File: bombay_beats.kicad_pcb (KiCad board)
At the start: 2 copper layers, 154.9 x 17.8 mm, 22 parts, among them SW1 SW_SPDT, U1 74HC165

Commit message: one sided version
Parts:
- added C1: 0.1u, Capacitor_SMD:C_0201_0603Metric, F.Cu at (129.5, 81.3)
- SW1, U1, jst_in1, jst_out1, solder_in1, solder_out1: moved to F.Cu
- moved SW1 38.2 mm to (132.3, 86.2), turned to 0 degrees
- moved R8 14.4 mm to (185.3, 76.8)
- moved btn_8 14.4 mm to (182.6, 85.0)
- moved solder_in1 12.5 mm to (194.0, 76.7), turned to 0 degrees
- moved btn_1 12.3 mm to (82.0, 85.0)
- moved R1 12.3 mm to (84.7, 76.8)
- moved jst_out1 12.0 mm to (60.9, 81.8), turned to -90 degrees
- moved jst_in1 9.95 mm to (203.7, 81.9), turned to 90 degrees
- moved R7 9.41 mm to (172.1, 76.8)
- moved btn_7 9.41 mm to (169.4, 85.0)
- moved solder_out1 9.32 mm to (69.5, 76.7), turned to 0 degrees
- moved R2 7.32 mm to (97.9, 76.8)
- moved btn_2 7.32 mm to (95.2, 85.0)
- moved U1 5.09 mm to (132.5, 77.7)
- moved R6 4.48 mm to (158.9, 76.8)
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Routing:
- net VCC: track 198.2 -> 328.8 mm, vias 3 -> 2
- net /DATA_IN: track 37.7 -> 78.8 mm
- net Net-(SW1-B): track 52.2 -> 19.9 mm
- net /DATA_CLK: track 171.7 -> 153.9 mm, vias 4 -> 0
- net /DATA_LOAD: track 162.8 -> 146.5 mm, vias 5 -> 2
- net GND: track 52.8 -> 37.4 mm, vias 8 -> 13
- net /Button Module/data: track 65.9 -> 51.9 mm, vias 1 -> 2
- net /Button Module7/data: track 59.1 -> 49.6 mm, vias 1 -> 0
- net /Button Module1/data: track 47.1 -> 38.3 mm, vias 1 -> 2
- net /Button Module6/data: track 40.7 -> 34.3 mm, vias 1 -> 0
- net /DATA_OUT: track 82.4 -> 86.4 mm
- net /Button Module2/data: track 28.6 -> 24.8 mm, vias 1 -> 2
- net /Button Module5/data: track 22.2 -> 19.6 mm, vias 1 -> 0
- net /Button Module3/data: track 10.1 -> 12.0 mm, vias 1 -> 0
- net /Button Module4/data: track 4.81 -> 4.69 mm, vias 1 -> 0

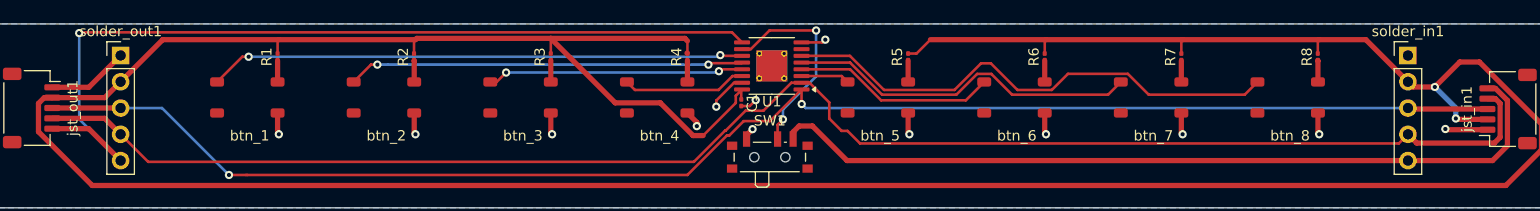
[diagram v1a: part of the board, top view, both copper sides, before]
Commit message: finalize one sided smd version
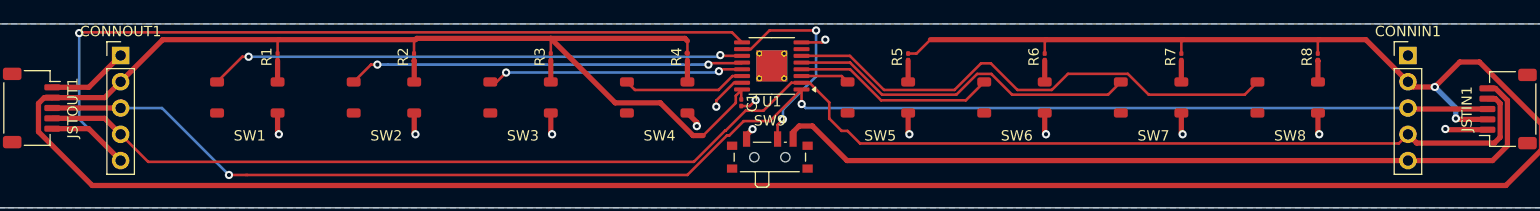
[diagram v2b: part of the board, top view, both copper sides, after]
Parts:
- renumbered solder_in1 to CONNIN1, solder_out1 to CONNOUT1, jst_in1 to JSTIN1, jst_out1 to JSTOUT1, btn_1 to SW1, btn_2 to SW2, btn_3 to SW3, btn_4 to SW4, btn_5 to SW5, btn_6 to SW6, btn_7 to SW7, btn_8 to SW8, SW1 to SW9

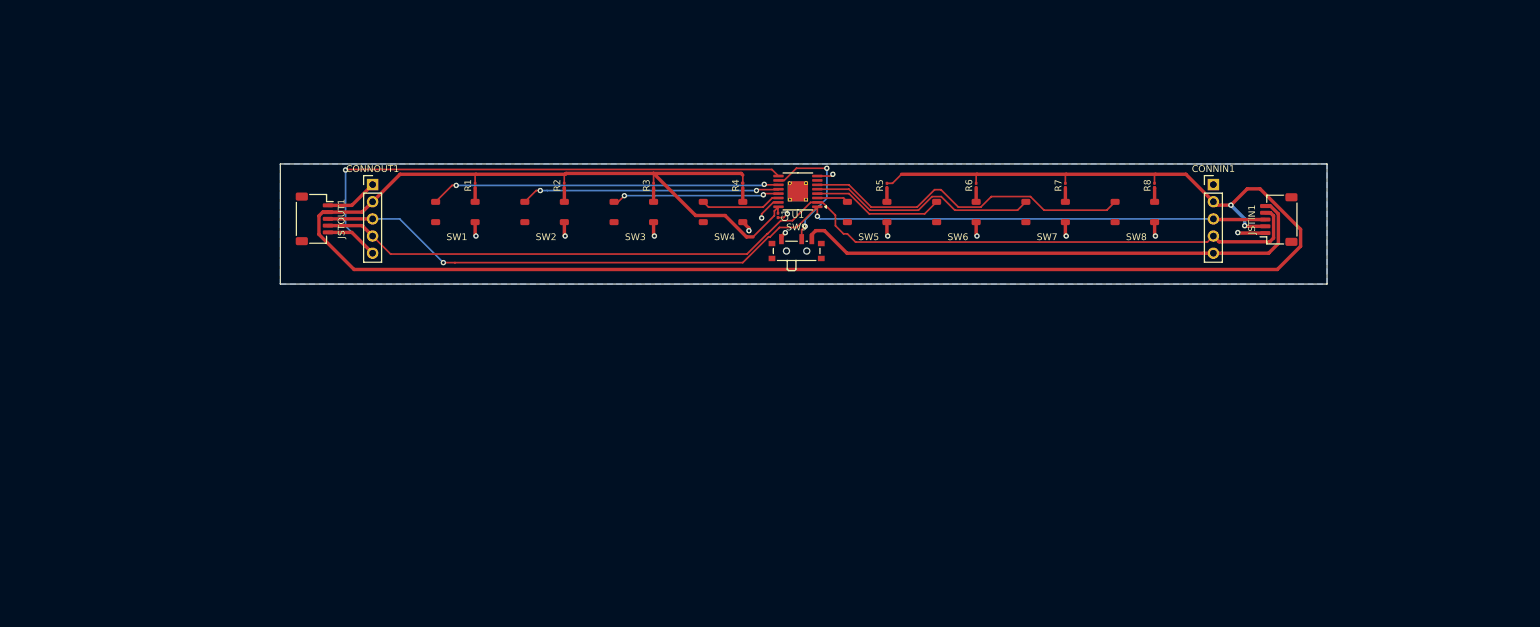
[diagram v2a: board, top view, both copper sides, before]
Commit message: replace footprints for through hole version
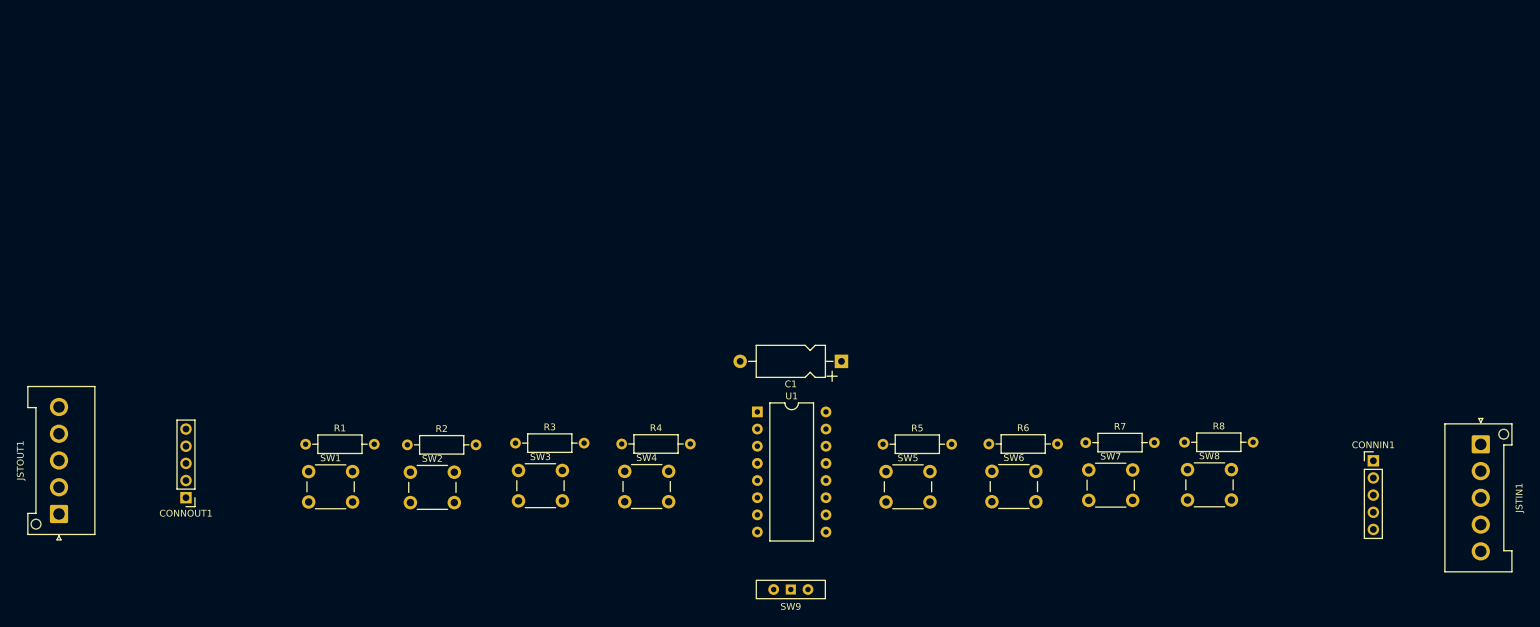
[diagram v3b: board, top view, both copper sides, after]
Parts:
- C1: footprint Capacitor_SMD:C_0201_0603Metric -> Capacitor_THT:CP_Axial_L10.0mm_D4.5mm_P15.00mm_Horizontal
- JSTIN1, JSTOUT1: footprint Connector_JST:JST_SH_SM05B-SRSS-TB_1x05-1MP_P1.00mm_Horizontal -> Connector_JST:JST_VH_B5P-VH-FB-B_1x05_P3.96mm_Vertical
- R1, R2, R3, R4, R5, R6, R7, R8: footprint Resistor_SMD:R_0201_0603Metric -> Resistor_THT:R_Axial_DIN0207_L6.3mm_D2.5mm_P10.16mm_Horizontal
- SW1, SW2, SW3, SW4, SW5, SW6, SW7, SW8: footprint CustomFootprints:4.5 Push Button Switch JLCPCB -> Button_Switch_THT:SW_PUSH_6mm_H4.3mm
- SW9: footprint Button_Switch_SMD:SW_SPDT_PCM12 -> Button_Switch_THT:SW_Slide-03_Wuerth-WS-SLTV_10x2.5x6.4_P2.54mm
- U1: footprint Package_SO:TSSOP-16-1EP_4.4x5mm_P0.65mm_EP3x3mm_ThermalVias -> Package_DIP:DIP-16_W10.16mm
- moved JSTOUT1 57.8 mm to (23.1, 125.5), turned to 90 degrees
- moved CONNOUT1 54.0 mm to (41.9, 123.1), turned to 180 degrees
- moved SW9 50.4 mm to (131.4, 136.7), turned to 180 degrees
- moved CONNIN1 47.3 mm to (217.7, 117.6)
- moved R1 45.8 mm to (59.6, 115.1), turned to 0 degrees
- moved R2 44.9 mm to (74.7, 115.2), turned to 0 degrees
- moved JSTIN1 44.7 mm to (233.6, 115.2), turned to -90 degrees
- moved R3 43.3 mm to (90.7, 115.0), turned to 0 degrees
- moved R4 42.3 mm to (106.4, 115.1), turned to 0 degrees
- moved SW1 40.7 mm to (60.1, 119.2)
- moved SW2 39.8 mm to (75.1, 119.3)
- moved R6 38.3 mm to (160.8, 115.1), turned to 0 degrees
- moved R5 38.3 mm to (145.1, 115.1), turned to 0 degrees
- moved R8 38.3 mm to (189.7, 114.9), turned to 0 degrees
- moved SW3 38.2 mm to (91.1, 119.0)
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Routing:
- net VCC: track 328.8 -> 0.00 mm, vias 2 -> 0
- net /DATA_CLK: track 153.9 -> 0.00 mm
- net /DATA_LOAD: track 146.5 -> 0.00 mm, vias 2 -> 0
- net /DATA_OUT: track 86.4 -> 0.00 mm, vias 1 -> 0
- net /DATA_IN: track 78.8 -> 0.00 mm
- net /Button Module/data: track 51.9 -> 0.00 mm, vias 2 -> 0
- net /Button Module7/data: track 49.6 -> 0.00 mm
- net /Button Module1/data: track 38.3 -> 0.00 mm, vias 2 -> 0
- net GND: track 37.4 -> 0.00 mm, vias 13 -> 0
- net /Button Module6/data: track 34.3 -> 0.00 mm
- net /Button Module2/data: track 24.8 -> 0.00 mm, vias 2 -> 0
- net Net-(SW9-B): track 19.9 -> 0.00 mm, vias 2 -> 0
- net /Button Module5/data: track 19.6 -> 0.00 mm
- net /Button Module3/data: track 12.0 -> 0.00 mm
- net /Button Module4/data: track 4.69 -> 0.00 mm
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- removed copper zone on B.Cu, net GND
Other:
- board outline removed

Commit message: production files
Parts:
- JSTIN1, JSTOUT1: footprint Connector_JST:JST_VH_B5P-VH-FB-B_1x05_P3.96mm_Vertical -> Connector_PinHeader_1.00mm:PinHeader_1x05_P1.00mm_Vertical
- SW1, SW2, SW3, SW4, SW5, SW6, SW7, SW8: footprint Button_Switch_THT:SW_PUSH_6mm_H4.3mm -> Button_Switch_THT:SW_PUSH_6mm_4Pin
- moved SW9 81.7 mm to (129.8, 55.0), turned to 0 degrees
- moved JSTOUT1 74.1 mm to (51.0, 56.9)
- moved CONNIN1 71.6 mm to (182.2, 55.4), turned to 90 degrees
- moved CONNOUT1 70.8 mm to (67.2, 56.9), turned to 90 degrees
- moved JSTIN1 66.5 mm to (204.6, 55.4), turned to 90 degrees
- moved R1 50.5 mm to (49.1, 65.8)
- moved R8 50.2 mm to (200.3, 65.8)
- moved R2 50.1 mm to (67.0, 65.8)
- moved C1 49.9 mm to (116.3, 58.4)
- moved R7 49.7 mm to (182.4, 65.8)
- moved R3 49.5 mm to (85.0, 65.8)
- moved R6 49.5 mm to (164.4, 65.8)
- moved R4 49.5 mm to (102.9, 65.8)
- moved R5 49.4 mm to (146.4, 65.8)
- moved SW8 42.2 mm to (208.7, 81.0), turned to 180 degrees
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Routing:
- net VCC: track 0.00 -> 312.3 mm
- net /DATA_LOAD: track 0.00 -> 192.1 mm, vias 0 -> 4
- net /DATA_CLK: track 0.00 -> 184.2 mm, vias 0 -> 4
- net /DATA_IN: track 0.00 -> 80.5 mm, vias 0 -> 1
- net /Button Module7/data: track 0.00 -> 78.9 mm
- net /DATA_OUT: track 0.00 -> 75.2 mm, vias 0 -> 3
- net /Button Module/data: track 0.00 -> 72.3 mm
- net /Button Module6/data: track 0.00 -> 59.9 mm
- net /Button Module1/data: track 0.00 -> 53.4 mm
- net /Button Module5/data: track 0.00 -> 41.7 mm
- net /Button Module2/data: track 0.00 -> 34.3 mm
- net /Button Module4/data: track 0.00 -> 21.9 mm
- net Net-(R8-Pad1): track 0.00 -> 16.0 mm
- net Net-(R7-Pad1): track 0.00 -> 16.0 mm
- net Net-(R6-Pad1): track 0.00 -> 16.0 mm
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- added copper zone on B.Cu, net GND
